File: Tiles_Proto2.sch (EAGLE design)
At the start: 44 parts, among them J1 7p-SMD-2.54, U1 ADXL345BCCZ-RL, U2 MPR121QR2, U3 MCP73832T-2ACI/OT-SOT23-5

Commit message: first draft board
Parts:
- removed SW2: (no value), Seeed-OPL-Switch:SMD-SWITCHES-TOP-4BIT(8P-11.8X6.8MM)
- added SJ3, SJ4, SJ5, SJ6: JUMPER-PAD-2-NO, SparkFun-Passives:JUMPER-PAD-2-NO
- renumbered - to B-, MOTOR+ to M+, MOTOR- to M-
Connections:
- net GND: now also SJ4.1; no longer SW2.2
- net N$13: now also SJ4.2; no longer SW2.7
- net N$14: now also SJ5.2; no longer SW2.6
- net N$15: now also SJ6.2; no longer SW2.5
- net N$6: now also SJ3.2; no longer SW2.8
- net SCL: now also SJ5.1; no longer SW2.3
- net SDA: now also SJ6.1; no longer SW2.4
- net VCC: now also SJ3.1; no longer SW2.1
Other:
- moved on the sheet: R1, R2, R3
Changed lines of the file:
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@@
 <part name="R6" library="Seeed-OPL-Resistor" deviceset="SMD-RES-10K-1%-1/10W(0603)" device="" value="10K"/>
 <part name="R7" library="Seeed-OPL-Resistor" deviceset="SMD-RES-10K-1%-1/10W(0603)" device="" value="10K"/>
-<part name="MOTOR+" library="wirepad" deviceset="SMD2" device=""/>
-<part name="MOTOR-" library="wirepad" deviceset="SMD2" device=""/>
+<part name="M+" library="wirepad" deviceset="SMD2" device=""/>
+<part name="M-" library="wirepad" deviceset="SMD2" device=""/>
 <part name="U$4" library="Seeed-OPL-Transistor" deviceset="SMD-TRANSISTORS-NPN-40V-200MA-MMBT3904LT1G(SOT-23)" device="" value="MMBT3904LT1G"/>
 <part name="GND2" library="SparkFun-Aesthetics" deviceset="GND" device=""/>
@@
 <part name="J1" library="Seeed-OPL-Connector" deviceset="SMD-BLACK-FEMALE-HEADER(7P-2.54)" device="" value="7p-SMD-2.54"/>
 <part name="B+" library="wirepad" deviceset="SMD2" device=""/>
-<part name="-" library="wirepad" deviceset="SMD2" device=""/>
+<part name="B-" library="wirepad" deviceset="SMD2" device=""/>
 <part name="GND8" library="SparkFun-Aesthetics" deviceset="GND" device=""/>
 <part name="D2" library="Seeed-OPL-Diode" deviceset="SMD-DIODE-100V-200MA(SOD-123)" device="" value="MMSD4148-sod123"/>
@@
 <part name="GND15" library="SparkFun-Aesthetics" deviceset="GND" device=""/>
 <part name="GND16" library="SparkFun-Aesthetics" deviceset="GND" device=""/>
-<part name="SW2" library="Seeed-OPL-Switch" deviceset="SMD-SWITCHES-TOP-4BIT(8P-11.8X6.8MM)" device=""/>
 <part name="JP1" library="SparkFun-Connectors" deviceset="M04" device="PTH"/>
 <part name="SUPPLY8" library="SparkFun-Aesthetics" deviceset="VCC" device=""/>
@@
 <part name="SJ1" library="SparkFun-Passives" deviceset="JUMPER-PAD-2-NC_BY_TRACE" device=""/>
 <part name="SJ2" library="SparkFun-Passives" deviceset="JUMPER-PAD-2-NC_BY_TRACE" device=""/>
+<part name="SJ3" library="SparkFun-Passives" deviceset="JUMPER-PAD-2-NO" device=""/>
+<part name="SJ4" library="SparkFun-Passives" deviceset="JUMPER-PAD-2-NO" device=""/>
+<part name="SJ5" library="SparkFun-Passives" deviceset="JUMPER-PAD-2-NO" device=""/>
+<part name="SJ6" library="SparkFun-Passives" deviceset="JUMPER-PAD-2-NO" device=""/>
 </parts>
 <sheets>
@@
 <instance part="U1" gate="G$1" x="213.36" y="133.35"/>
 <instance part="U2" gate="G$1" x="226.06" y="62.23"/>
-<instance part="R1" gate="G$1" x="186.69" y="31.75"/>
-<instance part="R2" gate="G$1" x="186.69" y="24.13"/>
-<instance part="R3" gate="G$1" x="186.69" y="17.78"/>
+<instance part="R1" gate="G$1" x="186.69" y="27.94"/>
+<instance part="R2" gate="G$1" x="186.69" y="25.4"/>
+<instance part="R3" gate="G$1" x="186.69" y="22.86"/>
 <instance part="SUPPLY1" gate="G$1" x="175.26" y="160.02"/>
 <instance part="SUPPLY2" gate="G$1" x="157.48" y="92.71" rot="R90"/>
@@
 <instance part="R6" gate="G$1" x="180.34" y="85.09" rot="R90"/>
 <instance part="R7" gate="G$1" x="172.72" y="85.09" rot="R90"/>
-<instance part="MOTOR+" gate="1" x="88.9" y="153.67"/>
-<instance part="MOTOR-" gate="1" x="88.9" y="148.59"/>
+<instance part="M+" gate="1" x="88.9" y="153.67"/>
+<instance part="M-" gate="1" x="88.9" y="148.59"/>
 <instance part="U$4" gate="G$1" x="105.41" y="140.97"/>
 <instance part="GND2" gate="1" x="107.95" y="123.19"/>
@@
 <instance part="J1" gate="G$1" x="158.75" y="152.4"/>
 <instance part="B+" gate="1" x="50.8" y="157.48" rot="R270"/>
-<instance part="-" gate="1" x="58.42" y="157.48" rot="R270"/>
+<instance part="B-" gate="1" x="58.42" y="157.48" rot="R270"/>
 <instance part="GND8" gate="1" x="67.31" y="151.13" rot="R90"/>
 <instance part="D2" gate="G$1" x="50.8" y="139.7" rot="R270"/>
@@
 <instance part="GND15" gate="1" x="13.97" y="86.36" rot="R270"/>
 <instance part="GND16" gate="1" x="50.8" y="58.42"/>
-<instance part="SW2" gate="G$1" x="121.92" y="97.79" rot="R270"/>
 <instance part="JP1" gate="G$1" x="142.24" y="99.06" rot="R180"/>
 <instance part="SUPPLY8" gate="G$1" x="104.14" y="104.14"/>
@@
 <instance part="SJ1" gate="G$1" x="165.1" y="92.71"/>
 <instance part="SJ2" gate="G$1" x="175.26" y="149.86" rot="R90"/>
+<instance part="SJ3" gate="G$1" x="121.92" y="101.6"/>
+<instance part="SJ4" gate="G$1" x="121.92" y="99.06"/>
+<instance part="SJ5" gate="G$1" x="121.92" y="96.52"/>
+<instance part="SJ6" gate="G$1" x="121.92" y="93.98"/>
 </instances>
 <busses>
@@
 </segment>
 <segment>
-<pinref part="SW2" gate="G$1" pin="3"/>
 <wire x1="105.41" y1="96.52" x2="114.3" y2="96.52" width="0.1524" layer="91"/>
 <label x="105.41" y="96.52" size="1.778" layer="95"/>
+<pinref part="SJ5" gate="G$1" pin="1"/>
+<wire x1="114.3" y1="96.52" x2="116.84" y2="96.52" width="0.1524" layer="91"/>
 </segment>
 </net>
@@
 </segment>
 <segment>
-<pinref part="SW2" gate="G$1" pin="4"/>
 <wire x1="105.41" y1="93.98" x2="114.3" y2="93.98" width="0.1524" layer="91"/>
 <label x="105.41" y="93.98" size="1.778" layer="95"/>
+<pinref part="SJ6" gate="G$1" pin="1"/>
+<wire x1="114.3" y1="93.98" x2="116.84" y2="93.98" width="0.1524" layer="91"/>
 </segment>
 </net>
@@
 <label x="172.72" y="25.4" size="1.778" layer="95"/>
 <pinref part="R2" gate="G$1" pin="1"/>
-<wire x1="182.88" y1="24.13" x2="172.72" y2="25.4" width="0.1524" layer="91"/>
+<wire x1="182.88" y1="25.4" x2="172.72" y2="25.4" width="0.1524" layer="91"/>
 </segment>
 <segment>
@@
 <label x="172.72" y="27.94" size="1.778" layer="95"/>
 <pinref part="R1" gate="G$1" pin="1"/>
-<wire x1="182.88" y1="31.75" x2="172.72" y2="27.94" width="0.1524" layer="91"/>
+<wire x1="182.88" y1="27.94" x2="172.72" y2="27.94" width="0.1524" layer="91"/>
 </segment>
 <segment>
@@
 <label x="172.72" y="22.86" size="1.778" layer="95"/>
 <pinref part="R3" gate="G$1" pin="1"/>
-<wire x1="182.88" y1="17.78" x2="172.72" y2="22.86" width="0.1524" layer="91"/>
+<wire x1="182.88" y1="22.86" x2="172.72" y2="22.86" width="0.1524" layer="91"/>
 </segment>
 </net>
@@
 <pinref part="D1" gate="G$1" pin="G+"/>
 <pinref part="R1" gate="G$1" pin="2"/>
-<wire x1="190.5" y1="31.75" x2="195.58" y2="27.94" width="0.1524" layer="91"/>
+<wire x1="190.5" y1="27.94" x2="195.58" y2="27.94" width="0.1524" layer="91"/>
 </segment>
 </net>
@@
 <pinref part="D1" gate="G$1" pin="R+"/>
 <pinref part="R2" gate="G$1" pin="2"/>
-<wire x1="190.5" y1="24.13" x2="195.58" y2="25.4" width="0.1524" layer="91"/>
+<wire x1="190.5" y1="25.4" x2="195.58" y2="25.4" width="0.1524" layer="91"/>
 </segment>
 </net>
@@
 <pinref part="D1" gate="G$1" pin="B+"/>
 <pinref part="R3" gate="G$1" pin="2"/>
-<wire x1="190.5" y1="17.78" x2="195.58" y2="22.86" width="0.1524" layer="91"/>
+<wire x1="190.5" y1="22.86" x2="195.58" y2="22.86" width="0.1524" layer="91"/>
 </segment>
 </net>
@@
 </segment>
 <segment>
-<pinref part="-" gate="1" pin="P"/>
+<pinref part="B-" gate="1" pin="P"/>
 <wire x1="58.42" y1="154.94" x2="58.42" y2="151.13" width="0.1524" layer="91"/>
 <pinref part="GND8" gate="1" pin="GND"/>
@@
 <pinref part="GND17" gate="1" pin="GND"/>
 <wire x1="104.14" y1="90.17" x2="104.14" y2="99.06" width="0.1524" layer="91"/>
-<pinref part="SW2" gate="G$1" pin="2"/>
 <wire x1="104.14" y1="99.06" x2="114.3" y2="99.06" width="0.1524" layer="91"/>
+<pinref part="SJ4" gate="G$1" pin="1"/>
+<wire x1="114.3" y1="99.06" x2="116.84" y2="99.06" width="0.1524" layer="91"/>
 </segment>
 </net>
@@
 </segment>
 <segment>
-<pinref part="MOTOR+" gate="1" pin="P"/>
+<pinref part="M+" gate="1" pin="P"/>
 <wire x1="91.44" y1="153.67" x2="111.76" y2="153.67" width="0.1524" layer="91"/>
 <pinref part="SUPPLY3" gate="G$1" pin="VCC"/>
@@
 <pinref part="SUPPLY8" gate="G$1" pin="VCC"/>
 <wire x1="104.14" y1="104.14" x2="104.14" y2="101.6" width="0.1524" layer="91"/>
-<pinref part="SW2" gate="G$1" pin="1"/>
 <wire x1="104.14" y1="101.6" x2="114.3" y2="101.6" width="0.1524" layer="91"/>
+<pinref part="SJ3" gate="G$1" pin="1"/>
+<wire x1="114.3" y1="101.6" x2="116.84" y2="101.6" width="0.1524" layer="91"/>
 </segment>
 <segment>
@@
 <net name="N$7" class="0">
 <segment>
-<pinref part="MOTOR-" gate="1" pin="P"/>
+<pinref part="M-" gate="1" pin="P"/>
 <wire x1="91.44" y1="148.59" x2="107.95" y2="148.59" width="0.1524" layer="91"/>
 <pinref part="U$4" gate="G$1" pin="C"/>
@@
 <net name="N$6" class="0">
 <segment>
-<pinref part="SW2" gate="G$1" pin="8"/>
 <pinref part="JP1" gate="G$1" pin="1"/>
 <wire x1="129.54" y1="101.6" x2="137.16" y2="101.6" width="0.1524" layer="91"/>
+<pinref part="SJ3" gate="G$1" pin="2"/>
+<wire x1="127" y1="101.6" x2="129.54" y2="101.6" width="0.1524" layer="91"/>
 </segment>
 </net>
 <net name="N$13" class="0">
 <segment>
-<pinref part="SW2" gate="G$1" pin="7"/>
 <pinref part="JP1" gate="G$1" pin="2"/>
 <wire x1="129.54" y1="99.06" x2="137.16" y2="99.06" width="0.1524" layer="91"/>
+<pinref part="SJ4" gate="G$1" pin="2"/>
+<wire x1="127" y1="99.06" x2="129.54" y2="99.06" width="0.1524" layer="91"/>
 </segment>
 </net>
 <net name="N$14" class="0">
 <segment>
-<pinref part="SW2" gate="G$1" pin="6"/>
 <pinref part="JP1" gate="G$1" pin="3"/>
 <wire x1="129.54" y1="96.52" x2="137.16" y2="96.52" width="0.1524" layer="91"/>
+<pinref part="SJ5" gate="G$1" pin="2"/>
+<wire x1="127" y1="96.52" x2="129.54" y2="96.52" width="0.1524" layer="91"/>
 </segment>
 </net>
 <net name="N$15" class="0">
 <segment>
-<pinref part="SW2" gate="G$1" pin="5"/>
 <pinref part="JP1" gate="G$1" pin="4"/>
 <wire x1="129.54" y1="93.98" x2="137.16" y2="93.98" width="0.1524" layer="91"/>
-</segment>
-</net>
+<pinref part="SJ6" gate="G$1" pin="2"/>
+<wire x1="127" y1="93.98" x2="129.54" y2="93.98" width="0.1524" layer="91"/>
+</segment>
+</net>

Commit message: version before starting routing
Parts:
- removed USB1: 10118193-0001LF, Seeed-OPL-Connector:MICRO-USB-SMD-B-(10118193-0001LF)
- added RFDUINO: RF22301, GeekAmmo:RF22301
- U$1: value RF22301 -> ST-USB-001L5; device GeekAmmo:RF22301 -> Seeed-OPL-Connector:MICRO-USB-AB-TYPE-180(ST-USB-001L5)
- renumbered CAP7 to CP7, CAP8 to CP8, CAP9 to CP9
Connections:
- net FACTORY: now also RFDUINO.FACT; no longer U$1.FACT
- net GND: now also R1.2, R2.2, R3.2, RFDUINO.GND@1, RFDUINO.GND@10, RFDUINO.GND@12, RFDUINO.GND@18, RFDUINO.GND@19, RFDUINO.GND@2, RFDUINO.GND@8, RFDUINO.GND@9, U$1.GND; no longer D1.B-, D1.G-, D1.R-, U$1.GND@1, U$1.GND@10, U$1.GND@12, U$1.GND@18, U$1.GND@19, U$1.GND@2, U$1.GND@8, U$1.GND@9, USB1.GND@5
- net HAPTIC: now also RFDUINO.GPIO3; no longer U$1.GPIO3
- net INT: now also RFDUINO.GPIO4; no longer U$1.GPIO4
- net LED_B: now also D1.B+, RFDUINO.GPIO2; no longer R3.1, U$1.GPIO2
- net LED_G: now also D1.G+, RFDUINO.GPIO1; no longer R1.1, U$1.GPIO1
- net LED_R: now also D1.R+, RFDUINO.GPIO0/AREF; no longer R2.1, U$1.GPIO0/AREF
- net N$1: now also D1.G-, R1.1; no longer D1.G+, R1.2
- net N$2: now also D1.R-, R2.1; no longer D1.R+, R2.2
- net N$3: now also D1.B-, R3.1; no longer D1.B+, R3.2
- net N$8: now also U$1.VCC; no longer USB1.VCC
- net RESET: now also RFDUINO.RESET; no longer U$1.RESET
- net SCL: now also RFDUINO.GPIO5; no longer U$1.GPIO5
- net SDA: now also RFDUINO.GPIO6; no longer U$1.GPIO6
- net VCC: now also RFDUINO.3V; no longer U$1.3V
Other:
- moved on the sheet: R1, R2, R3

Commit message: routing in progress
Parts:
- removed U$1: ST-USB-001L5, Seeed-OPL-Connector:MICRO-USB-AB-TYPE-180(ST-USB-001L5)
- added USB1: 10118193-0001LF, Seeed-OPL-Connector:MICRO-USB-SMD-B-(10118193-0001LF)
- renumbered U$4 to Q1
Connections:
- net GND: now also USB1.GND@5; no longer U$1.GND
- net N$8: now also USB1.VCC; no longer U$1.VCC
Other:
- moved on the sheet: C5
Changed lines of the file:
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@@
 <setting verticaltext="up"/>
 </settings>
-<grid distance="0.1" unitdist="inch" unit="inch" style="lines" multiple="1" display="yes" altdistance="0.01" altunitdist="inch" altunit="inch"/>
+<grid distance="0.1" unitdist="inch" unit="inch" style="lines" multiple="1" display="no" altdistance="0.01" altunitdist="inch" altunit="inch"/>
 <layers>
 <layer number="1" name="Top" color="4" fill="1" visible="no" active="no"/>
@@
 <part name="M+" library="wirepad" deviceset="SMD2" device=""/>
 <part name="M-" library="wirepad" deviceset="SMD2" device=""/>
-<part name="U$4" library="Seeed-OPL-Transistor" deviceset="SMD-TRANSISTORS-NPN-40V-200MA-MMBT3904LT1G(SOT-23)" device="" value="MMBT3904LT1G"/>
+<part name="Q1" library="Seeed-OPL-Transistor" deviceset="SMD-TRANSISTORS-NPN-40V-200MA-MMBT3904LT1G(SOT-23)" device="" value="MMBT3904LT1G"/>
 <part name="GND2" library="SparkFun-Aesthetics" deviceset="GND" device=""/>
 <part name="R8" library="Seeed-OPL-Resistor" deviceset="SMD-RES-10K-1%-1/10W(0603)" device="" value="10K"/>
@@
 <part name="SJ5" library="SparkFun-Passives" deviceset="JUMPER-PAD-2-NO" device=""/>
 <part name="SJ6" library="SparkFun-Passives" deviceset="JUMPER-PAD-2-NO" device=""/>
-<part name="U$1" library="Seeed-OPL-Connector" deviceset="MICRO-USB-AB-TYPE-180(ST-USB-001L5)" device="" value="ST-USB-001L5"/>
+<part name="USB1" library="Seeed-OPL-Connector" deviceset="MICRO-USB-SMD-B-(10118193-0001LF)" device="" value="10118193-0001LF"/>
 </parts>
 <sheets>
@@
 <instance part="M+" gate="1" x="88.9" y="153.67"/>
 <instance part="M-" gate="1" x="88.9" y="148.59"/>
-<instance part="U$4" gate="G$1" x="105.41" y="140.97"/>
+<instance part="Q1" gate="G$1" x="105.41" y="140.97"/>
 <instance part="GND2" gate="1" x="107.95" y="123.19"/>
 <instance part="R8" gate="G$1" x="96.52" y="133.35" rot="R90"/>
@@
 <instance part="SW1" gate="G$1" x="26.67" y="151.13"/>
 <instance part="U3" gate="G$1" x="95.25" y="26.67" rot="R180"/>
-<instance part="C5" gate="G$1" x="46.99" y="16.51" rot="R90"/>
+<instance part="C5" gate="G$1" x="45.72" y="16.51" rot="R90"/>
 <instance part="C6" gate="G$1" x="127" y="20.32" rot="R90"/>
 <instance part="R9" gate="G$1" x="59.69" y="21.59" rot="R270"/>
 <instance part="R10" gate="G$1" x="76.2" y="12.7" rot="R90"/>
 <instance part="D3" gate="G$1" x="59.69" y="11.43" rot="R270"/>
-<instance part="GND10" gate="1" x="39.37" y="13.97"/>
-<instance part="GND11" gate="1" x="46.99" y="0"/>
+<instance part="GND10" gate="1" x="38.1" y="12.7"/>
+<instance part="GND11" gate="1" x="45.72" y="0"/>
 <instance part="GND12" gate="1" x="76.2" y="0"/>
 <instance part="GND13" gate="1" x="127" y="0"/>
@@
 <instance part="SJ5" gate="G$1" x="121.92" y="96.52"/>
 <instance part="SJ6" gate="G$1" x="121.92" y="93.98"/>
-<instance part="U$1" gate="G$1" x="21.59" y="26.67"/>
+<instance part="USB1" gate="G$1" x="20.32" y="30.48"/>
 </instances>
 <busses>
@@
 </segment>
 <segment>
-<pinref part="U$4" gate="G$1" pin="E"/>
+<pinref part="Q1" gate="G$1" pin="E"/>
 <pinref part="GND2" gate="1" pin="GND"/>
 <wire x1="107.95" y1="135.89" x2="107.95" y2="125.73" width="0.1524" layer="91"/>
@@
 <pinref part="C5" gate="G$1" pin="1"/>
 <pinref part="GND11" gate="1" pin="GND"/>
-<wire x1="46.99" y1="12.7" x2="46.99" y2="2.54" width="0.1524" layer="91"/>
+<wire x1="45.72" y1="12.7" x2="45.72" y2="2.54" width="0.1524" layer="91"/>
 </segment>
 <segment>
@@
 </segment>
 <segment>
-<pinref part="U$1" gate="G$1" pin="GND"/>
 <pinref part="GND10" gate="1" pin="GND"/>
-<wire x1="33.02" y1="21.59" x2="39.37" y2="21.59" width="0.1524" layer="91"/>
-<wire x1="39.37" y1="21.59" x2="39.37" y2="16.51" width="0.1524" layer="91"/>
+<wire x1="38.1" y1="20.32" x2="38.1" y2="15.24" width="0.1524" layer="91"/>
+<wire x1="30.48" y1="25.4" x2="34.29" y2="25.4" width="0.1524" layer="91"/>
+<wire x1="34.29" y1="25.4" x2="38.1" y2="25.4" width="0.1524" layer="91"/>
+<wire x1="38.1" y1="25.4" x2="38.1" y2="20.32" width="0.1524" layer="91"/>
+<pinref part="USB1" gate="G$1" pin="GND@5"/>
 </segment>
 </net>
@@
 </segment>
 <segment>
-<pinref part="U$4" gate="G$1" pin="B"/>
+<pinref part="Q1" gate="G$1" pin="B"/>
 <wire x1="102.87" y1="140.97" x2="96.52" y2="140.97" width="0.1524" layer="91"/>
 <pinref part="R8" gate="G$1" pin="2"/>
@@
 <pinref part="M-" gate="1" pin="P"/>
 <wire x1="91.44" y1="148.59" x2="107.95" y2="148.59" width="0.1524" layer="91"/>
-<pinref part="U$4" gate="G$1" pin="C"/>
+<pinref part="Q1" gate="G$1" pin="C"/>
 <wire x1="107.95" y1="148.59" x2="107.95" y2="146.05" width="0.1524" layer="91"/>
 </segment>
@@
 <pinref part="U3" gate="G$1" pin="VDD"/>
 <pinref part="C5" gate="G$1" pin="2"/>
-<wire x1="46.99" y1="31.75" x2="59.69" y2="31.75" width="0.1524" layer="91"/>
+<wire x1="45.72" y1="31.75" x2="59.69" y2="31.75" width="0.1524" layer="91"/>
 <wire x1="59.69" y1="31.75" x2="80.01" y2="31.75" width="0.1524" layer="91"/>
-<wire x1="46.99" y1="31.75" x2="46.99" y2="20.32" width="0.1524" layer="91"/>
+<wire x1="45.72" y1="31.75" x2="45.72" y2="30.48" width="0.1524" layer="91"/>
 <pinref part="R9" gate="G$1" pin="1"/>
+<wire x1="45.72" y1="30.48" x2="45.72" y2="20.32" width="0.1524" layer="91"/>
 <wire x1="59.69" y1="31.75" x2="59.69" y2="25.4" width="0.1524" layer="91"/>
-<junction x="46.99" y="31.75"/>
+<junction x="45.72" y="31.75"/>
 <junction x="59.69" y="31.75"/>
-<pinref part="U$1" gate="G$1" pin="VCC"/>
-<wire x1="33.02" y1="31.75" x2="46.99" y2="31.75" width="0.1524" layer="91"/>
-</segment>
-</net>
+<wire x1="30.48" y1="35.56" x2="34.29" y2="35.56" width="0.1524" layer="91"/>
+<wire x1="34.29" y1="35.56" x2="45.72" y2="35.56" width="0.1524" layer="91"/>
+<wire x1="45.72" y1="35.56" x2="45.72" y2="30.48" width="0.1524" layer="91"/>
+<pinref part="USB1" gate="G$1" pin="VCC"/>
+</segment>
+</net>

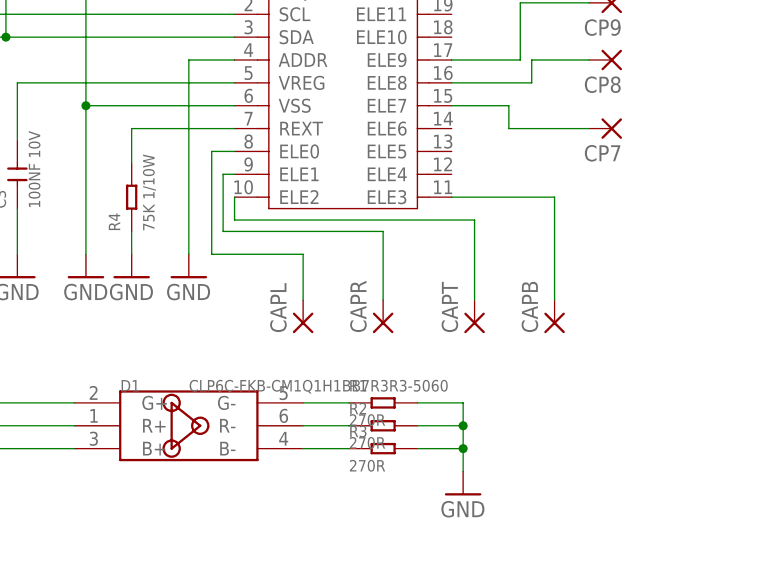
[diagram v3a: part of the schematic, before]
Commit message: finished silkscreen, no copper pour
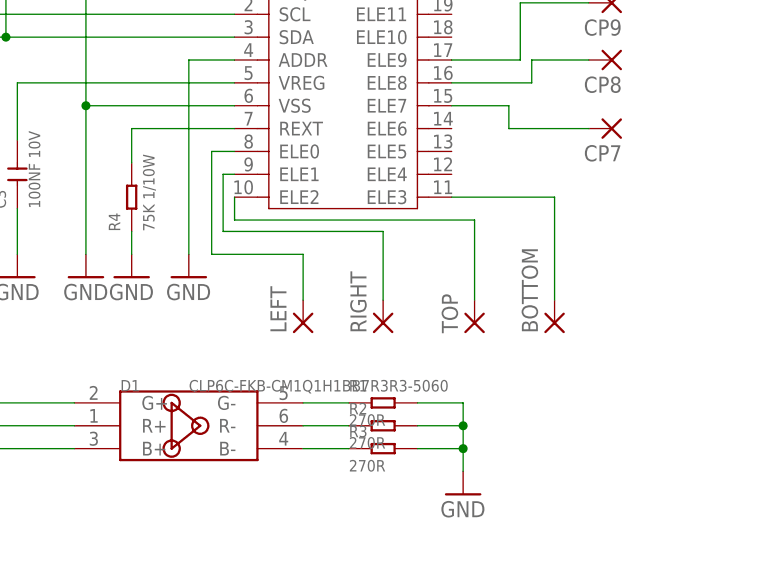
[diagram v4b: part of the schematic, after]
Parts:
- renumbered CAPB to BOTTOM, CAPL to LEFT, CAPR to RIGHT, CAPT to TOP
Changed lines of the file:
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@@
 <part name="R11" library="Seeed-OPL-Resistor" deviceset="SMD-RES-10K-1%-1/10W(0603)" device="" value="10K"/>
 <part name="R12" library="Seeed-OPL-Resistor" deviceset="SMD-RES-10K-1%-1/10W(0603)" device="" value="10K"/>
-<part name="CAPL" library="wirepad" deviceset="SMD5" device=""/>
-<part name="CAPR" library="wirepad" deviceset="SMD5" device=""/>
-<part name="CAPT" library="wirepad" deviceset="SMD5" device=""/>
-<part name="CAPB" library="wirepad" deviceset="SMD5" device=""/>
+<part name="LEFT" library="wirepad" deviceset="SMD5" device=""/>
+<part name="RIGHT" library="wirepad" deviceset="SMD5" device=""/>
+<part name="TOP" library="wirepad" deviceset="SMD5" device=""/>
+<part name="BOTTOM" library="wirepad" deviceset="SMD5" device=""/>
 <part name="CP7" library="wirepad" deviceset="SMD2" device=""/>
 <part name="CP8" library="wirepad" deviceset="SMD2" device=""/>
@@
 <instance part="R11" gate="G$1" x="241.3" y="149.86" rot="R90"/>
 <instance part="R12" gate="G$1" x="251.46" y="149.86" rot="R90"/>
-<instance part="CAPL" gate="1" x="220.98" y="36.83" rot="R90"/>
-<instance part="CAPR" gate="1" x="229.87" y="36.83" rot="R90"/>
-<instance part="CAPT" gate="1" x="240.03" y="36.83" rot="R90"/>
-<instance part="CAPB" gate="1" x="248.92" y="36.83" rot="R90"/>
+<instance part="LEFT" gate="1" x="220.98" y="36.83" rot="R90"/>
+<instance part="RIGHT" gate="1" x="229.87" y="36.83" rot="R90"/>
+<instance part="TOP" gate="1" x="240.03" y="36.83" rot="R90"/>
+<instance part="BOTTOM" gate="1" x="248.92" y="36.83" rot="R90"/>
 <instance part="CP7" gate="1" x="255.27" y="58.42" rot="R180"/>
 <instance part="CP8" gate="1" x="255.27" y="66.04" rot="R180"/>
@@
 <wire x1="210.82" y1="55.88" x2="210.82" y2="44.45" width="0.1524" layer="91"/>
 <wire x1="210.82" y1="44.45" x2="220.98" y2="44.45" width="0.1524" layer="91"/>
-<pinref part="CAPL" gate="1" pin="P"/>
+<pinref part="LEFT" gate="1" pin="P"/>
 <wire x1="220.98" y1="44.45" x2="220.98" y2="39.37" width="0.1524" layer="91"/>
 </segment>
@@
 <wire x1="212.09" y1="53.34" x2="212.09" y2="46.99" width="0.1524" layer="91"/>
 <wire x1="212.09" y1="46.99" x2="229.87" y2="46.99" width="0.1524" layer="91"/>
-<pinref part="CAPR" gate="1" pin="P"/>
+<pinref part="RIGHT" gate="1" pin="P"/>
 <wire x1="229.87" y1="46.99" x2="229.87" y2="39.37" width="0.1524" layer="91"/>
 </segment>
@@
 <wire x1="213.36" y1="50.8" x2="213.36" y2="48.26" width="0.1524" layer="91"/>
 <wire x1="213.36" y1="48.26" x2="240.03" y2="48.26" width="0.1524" layer="91"/>
-<pinref part="CAPT" gate="1" pin="P"/>
+<pinref part="TOP" gate="1" pin="P"/>
 <wire x1="240.03" y1="48.26" x2="240.03" y2="39.37" width="0.1524" layer="91"/>
 </segment>
@@
 <segment>
 <pinref part="U2" gate="G$1" pin="ELE3"/>
-<pinref part="CAPB" gate="1" pin="P"/>
+<pinref part="BOTTOM" gate="1" pin="P"/>
 <wire x1="237.49" y1="50.8" x2="248.92" y2="50.8" width="0.1524" layer="91"/>
 <wire x1="248.92" y1="50.8" x2="248.92" y2="39.37" width="0.1524" layer="91"/>
